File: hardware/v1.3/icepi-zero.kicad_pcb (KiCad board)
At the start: 4 copper layers, 65 x 30 mm, 160 parts, among them J1 Conn_02x20_Counter_Clockwise, J2 HDMI_C_1.3, J3 USB_C_Receptacle_USB2.0_14P, J4 USB_C_Receptacle_USB2.0_14P, J5 USB_C_Receptacle_USB2.0_14P, J6 Micro_SD_Card_Det2, SW1 SW_Push, SW2 SW_Push, U1 ECP5-CABGA256, U10 W9825G6KH, U11 W25Q128JVS, U2 TLV62569DBV, U3 TLV62569DBV, U4 TLV62569DBV, U5 PCA9306DC1, U6 FT231XQ, U7 TPD2EUSB30A, U8 TPD2EUSB30A, U9 TPD2EUSB30A, Y1 SG-8018CG 50.000000MHz

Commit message: Newest source files
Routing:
- net +3V3: track 95.9 -> 95.3 mm

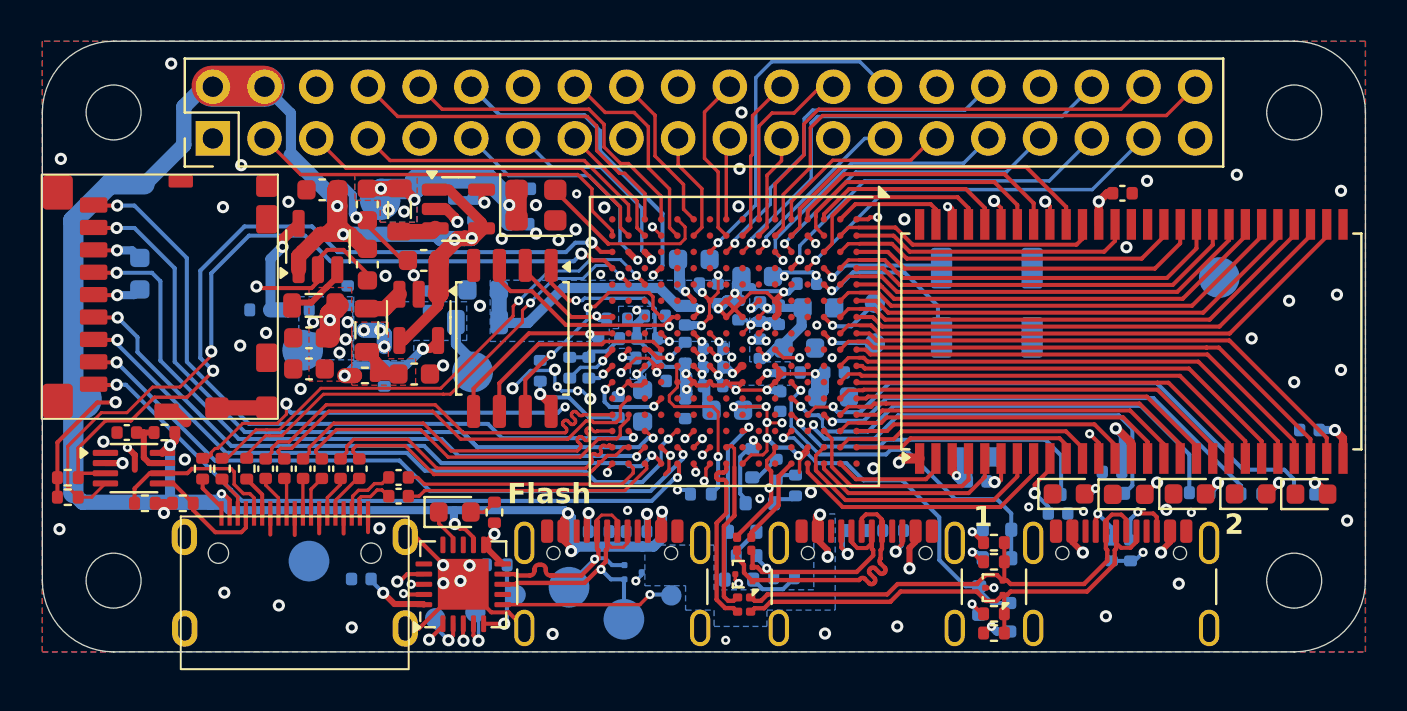
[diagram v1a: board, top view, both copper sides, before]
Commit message: Refine README
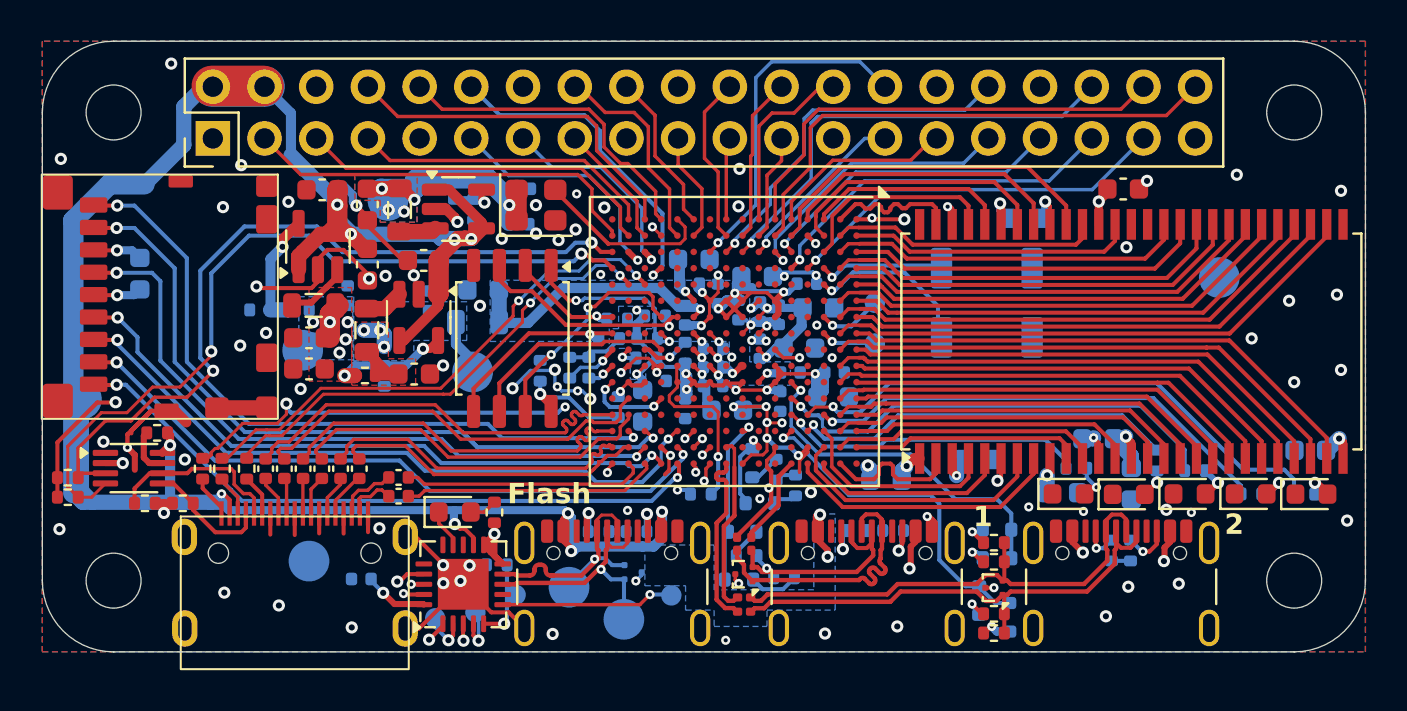
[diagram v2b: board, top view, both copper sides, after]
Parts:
- removed C37: 100pF, Capacitor_SMD:C_0402_1005Metric
- added C53: 22nF, Capacitor_SMD:C_0603_1608Metric, B.Cu at (164.2, 98.7)
- added C54: 22nF, Capacitor_SMD:C_0603_1608Metric, B.Cu at (157.4, 111.6)
- C39, C40, C41, C43, C44: value 100nF -> 22nF; footprint Capacitor_SMD:C_0402_1005Metric -> Capacitor_SMD:C_0603_1608Metric
- moved C42 7.66 mm to (169.5, 111.7), turned to -90 degrees
- moved R4 1.94 mm to (170.8, 110.6), turned to -90 degrees
- moved C40 1.77 mm to (167.9, 109.5)
- moved R1 1.31 mm to (166.8, 111.0)
- moved R2 1.10 mm to (172.6, 111.1)
- moved C43 1.08 mm to (162.0, 110.5)
- moved C41 1.04 mm to (166.1, 112.2)
- moved C39 1.00 mm to (178.3, 110.1)
- moved TP4 0.39 mm to (133.0, 97.8)
- moved R15 0.36 mm to (121.6, 109.2)
- moved C44 0.21 mm to (169.1, 97.3)
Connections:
- net FLASH_MISO renamed /Flash/FLASH_MISO
- net FLASH_MOSI renamed /Flash/FLASH_MOSI
- net JTAG_TCK renamed /USB/JTAG_TCK
- net JTAG_TDI renamed /USB/JTAG_TDI
- net JTAG_TDO renamed /USB/JTAG_TDO
- net JTAG_TMS renamed /USB/JTAG_TMS
- net ~{FLASH_CS} renamed /Flash/~{FLASH_CS}
- net ~{FLASH_RESET} renamed /Flash/~{FLASH_RESET}
- net ~{FLASH_WP} renamed /Flash/~{FLASH_WP}
- J1 pad 10: /GPIO4 -> /GPIO15
- J1 pad 11: /GPIO5 -> /GPIO17
- J1 pad 12: /GPIO6 -> /GPIO18
- J1 pad 13: /GPIO7 -> /GPIO27
- J1 pad 15: /GPIO8 -> /GPIO22
- J1 pad 16: /GPIO9 -> /GPIO23
- J1 pad 18: /GPIO10 -> /GPIO24
- J1 pad 19: /GPIO11 -> /GPIO10
- J1 pad 21: /GPIO12 -> /GPIO9
- J1 pad 22: /GPIO13 -> /GPIO25
- J1 pad 23: /GPIO14 -> /GPIO11
- J1 pad 24: /GPIO15 -> /GPIO8
- J1 pad 26: /GPIO16 -> /GPIO7
- J1 pad 27: /GPIO17 -> /GPIO0
- J1 pad 28: /GPIO18 -> /GPIO1
- J1 pad 29: /GPIO19 -> /GPIO5
- J1 pad 3: /GPIO0 -> /GPIO2
- J1 pad 31: /GPIO20 -> /GPIO6
- J1 pad 32: /GPIO21 -> /GPIO12
- J1 pad 33: /GPIO22 -> /GPIO13
- J1 pad 35: /GPIO23 -> /GPIO19
- J1 pad 36: /GPIO24 -> /GPIO16
- J1 pad 37: /GPIO25 -> /GPIO26
- J1 pad 38: /GPIO26 -> /GPIO20
- J1 pad 40: /GPIO27 -> /GPIO21
- J1 pad 5: /GPIO1 -> /GPIO3
- J1 pad 7: /GPIO2 -> /GPIO4
- J1 pad 8: /GPIO3 -> /GPIO14
- U1 pad D4: /GPIO25 -> /GPIO26
- U1 pad E1: /GPIO19 -> /GPIO5
- U1 pad E3: /GPIO22 -> /GPIO13
- U1 pad E4: /GPIO23 -> /GPIO19
- U1 pad F1: /GPIO26 -> /GPIO20
- U1 pad F2: /GPIO27 -> /GPIO21
- U1 pad F3: /GPIO20 -> /GPIO6
- U1 pad G1: /GPIO16 -> /GPIO7
- U1 pad G2: /GPIO14 -> /GPIO11
- U1 pad G3: /GPIO17 -> /GPIO0
- U1 pad H2: /GPIO15 -> /GPIO8
- U1 pad H3: /GPIO24 -> /GPIO16
- U1 pad J1: /GPIO12 -> /GPIO9
- U1 pad J2: /GPIO13 -> /GPIO25
- U1 pad J3: /GPIO21 -> /GPIO12
- U1 pad K3: /GPIO18 -> /GPIO1
- U1 pad L1: /GPIO10 -> /GPIO24
- U1 pad L2: /GPIO11 -> /GPIO10
- U1 pad M2: /GPIO9 -> /GPIO23
- U1 pad N1: /GPIO4 -> /GPIO15
- U1 pad N4: /GPIO6 -> /GPIO18
- U1 pad P1: /GPIO3 -> /GPIO14
- U1 pad P2: /GPIO8 -> /GPIO22
- U1 pad P3: /GPIO7 -> /GPIO27
- U1 pad R1: /GPIO2 -> /GPIO4
- U1 pad R2: /GPIO1 -> /GPIO3
- U1 pad R3: /GPIO5 -> /GPIO17
- U1 pad T2: /GPIO0 -> /GPIO2
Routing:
- net /GPIO27: track 25.8 -> 10.6 mm, vias 0 -> 1
- net /GPIO24: track 22.3 -> 7.88 mm, vias 1 -> 0
- net /GPIO12: track 3.80 -> 17.8 mm, vias 0 -> 1
- net /GPIO16: track 8.40 -> 22.3 mm, vias 0 -> 1
- net /GPIO14: track 5.24 -> 17.6 mm
- net /GPIO0: track 19.8 -> 8.72 mm, vias 0 -> 1
- net /GPIO25: track 19.1 -> 8.27 mm, vias 1 -> 0
- net /GPIO22: track 15.2 -> 6.18 mm, vias 1 -> 0
- net /GPIO19: track 9.09 -> 17.8 mm, vias 0 -> 1
- net /GPIO20: track 14.3 -> 22.7 mm, vias 1 -> 0
- net GND: track 90.4 -> 98.4 mm, vias 108 -> 109
- net /GPIO21: track 17.8 -> 25.8 mm, vias 1 -> 0
- net /GPIO15: track 8.11 -> 15.9 mm
- net /GPIO23: track 17.8 -> 10.1 mm, vias 1 -> 0
- net /GPIO13: track 8.27 -> 15.2 mm, vias 0 -> 1
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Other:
- board text added: "HDMI - 100ohm USB - 90ohm"
- board text added: "Icepi Zero v1.3"
- board text removed: "Icepi Zero v1.2"

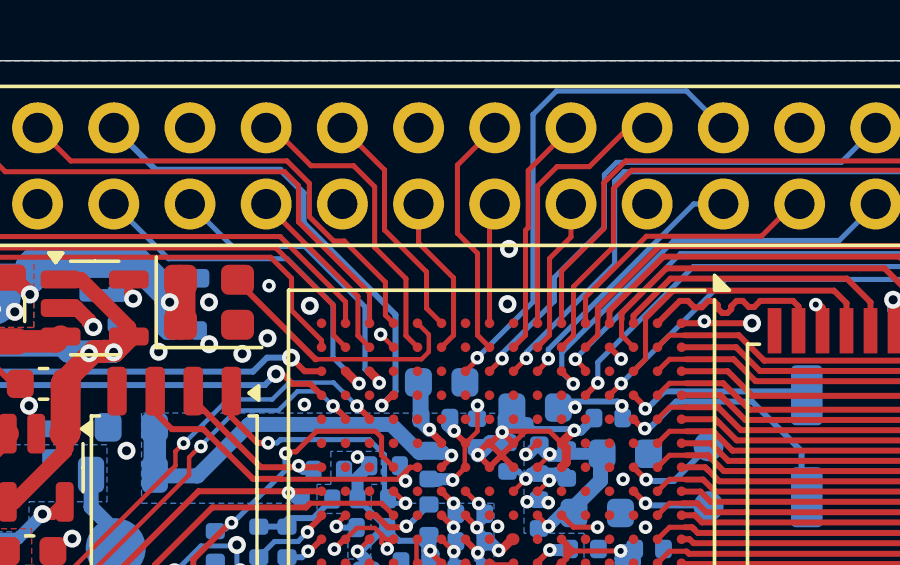
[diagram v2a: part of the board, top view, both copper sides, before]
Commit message: Change to more optimal inductor
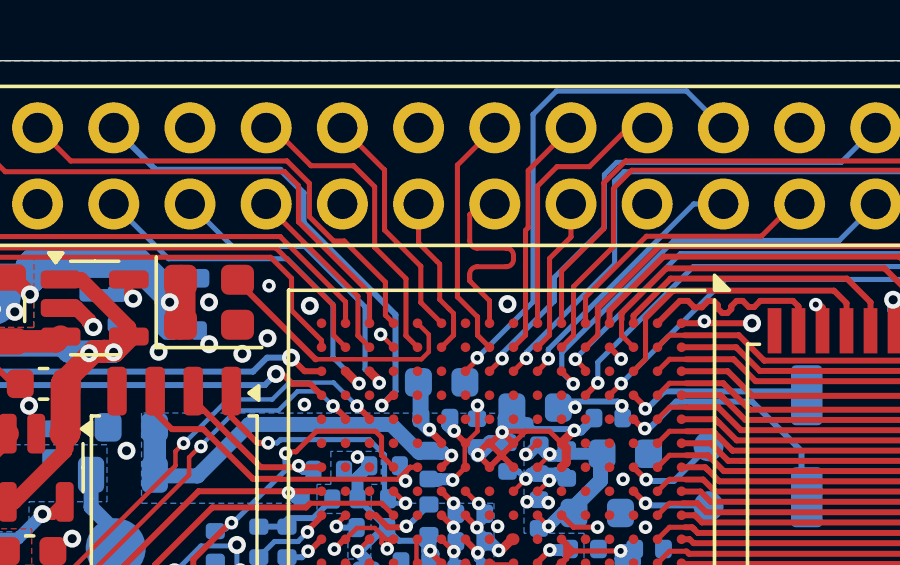
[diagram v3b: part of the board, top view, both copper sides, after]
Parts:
- L1, L2, L3: value 2.2uH -> 2.2uH 100mA+ 400mO-
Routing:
- net /GPIO9: track 3.80 -> 7.33 mm
- net GND: vias 109 -> 108
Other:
- board text added: "HDMI - 100ohm differential (coplanar waveguide 0.15mm) USB - 90ohm differential (coplanar waveguide 0.15mm)"
- board text removed: "HDMI - 100ohm USB - 90ohm"
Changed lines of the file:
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@@
 			)
 		)
-		(property "Value" "2.2uH"
+		(property "Value" "2.2uH 100mA+ 400mO-"
 			(at 0 1.55 0)
 			(layer "F.Fab")
@@
 			)
 		)
-		(property "LCSC Part #" "C1043"
+		(property "LCSC Part #" "C107322"
 			(at 0 0 0)
 			(unlocked yes)
@@
 			)
 		)
-		(property "LCSC Link" "https://lcsc.com/product-detail/Inductors-SMD_FH-CMI201209U2R2KT_C1043.html"
+		(property "LCSC Link" "https://lcsc.com/product-detail/C107322.html"
 			(at 0 0 0)
 			(unlocked yes)
@@
 			)
 		)
-		(property "Manufactuer Part Number" "CMI201209U2R2KT"
+		(property "Manufactuer Part Number" "TDK MLP2012S2R2MT0S1"
 			(at 0 0 0)
 			(unlocked yes)
@@
 			)
 		)
-		(property "Value" "2.2uH"
+		(property "Value" "2.2uH 100mA+ 400mO-"
 			(at 0 1.55 90)
 			(layer "F.Fab")
@@
 			)
 		)
-		(property "LCSC Part #" "C1043"
+		(property "LCSC Part #" "C107322"
 			(at 0 0 90)
 			(unlocked yes)
@@
 			)
 		)
-		(property "LCSC Link" "https://lcsc.com/product-detail/Inductors-SMD_FH-CMI201209U2R2KT_C1043.html"
+		(property "LCSC Link" "https://lcsc.com/product-detail/C107322.html"
 			(at 0 0 90)
 			(unlocked yes)
@@
 			)
 		)
-		(property "Manufactuer Part Number" "CMI201209U2R2KT"
+		(property "Manufactuer Part Number" "TDK MLP2012S2R2MT0S1"
 			(at 0 0 90)
 			(unlocked yes)
@@
 			)
 		)
-		(property "Value" "2.2uH"
+		(property "Value" "2.2uH 100mA+ 400mO-"
 			(at 0 1.55 90)
 			(layer "F.Fab")
@@
 			)
 		)
-		(property "LCSC Part #" "C1043"
+		(property "LCSC Part #" "C107322"
 			(at 0 0 270)
 			(unlocked yes)
@@
 			)
 		)
-		(property "LCSC Link" "https://lcsc.com/product-detail/Inductors-SMD_FH-CMI201209U2R2KT_C1043.html"
+		(property "LCSC Link" "https://lcsc.com/product-detail/C107322.html"
 			(at 0 0 270)
 			(unlocked yes)
@@
 			)
 		)
-		(property "Manufactuer Part Number" "CMI201209U2R2KT"
+		(property "Manufactuer Part Number" "TDK MLP2012S2R2MT0S1"
 			(at 0 0 270)
 			(unlocked yes)
@@
 		)
 	)
-	(gr_text "HDMI - 100ohm\nUSB - 90ohm"
+	(gr_text "HDMI - 100ohm differential (coplanar waveguide 0.15mm)\nUSB - 90ohm differential (coplanar waveguide 0.15mm)"
 		(at 150.59 88.93 0)
 		(layer "Cmts.User")
@@
 	)
 	(via
-		(at 150.25 96.27)
-		(size 0.6)
-		(drill 0.3)
-		(layers "F.Cu" "B.Cu")
-		(free yes)
-		(net 17)
-	)
-	(via
 		(at 167.15 113.1)
 		(size 0.45)
@@
 	)
 	(segment
-		(start 148.53 93.48)
-		(end 148.53 95.75)
+		(start 148.53 97.87)
+		(end 149.2 98.54)
 		(width 0.17)
 		(layer "F.Cu")
@@
 	)
 	(segment
-		(start 149.2 96.42)
-		(end 149.2 99.15)
+		(start 149.2 99.15)
+		(end 149.6 99.55)
 		(width 0.17)
 		(layer "F.Cu")
@@
 	)
 	(segment
-		(start 149.2 99.15)
-		(end 149.6 99.55)
+		(start 148.53 93.48)
+		(end 148.53 97.87)
 		(width 0.17)
 		(layer "F.Cu")
@@
 	)
 	(segment
-		(start 148.53 95.75)
-		(end 149.2 96.42)
+		(start 149.2 98.54)
+		(end 149.2 99.15)
 		(width 0.17)
 		(layer "F.Cu")
@@
 	)
 	(segment
-		(start 146.1 95.64)
-		(end 147.5 97.04)
+		(start 147.31 96.85)
+		(end 147.31 98.06)
 		(width 0.17)
 		(layer "F.Cu")
@@
 	)
 	(segment
-		(start 147.5 98.25)
-		(end 148 98.75)
+		(start 146.1 93.64)
+		(end 146.1 95.64)
 		(width 0.17)
 		(layer "F.Cu")
@@
 	)
 	(segment
-		(start 144.695 92.235)
-		(end 146.1 93.64)
+		(start 146.1 95.64)
+		(end 147.31 96.85)
 		(width 0.17)
 		(layer "F.Cu")
@@
 	)
 	(segment
-		(start 147.5 97.04)
-		(end 147.5 98.25)
+		(start 144.695 92.235)
+		(end 146.1 93.64)
 		(width 0.17)
 		(layer "F.Cu")
@@
 	)
 	(segment
-		(start 146.1 93.64)
-		(end 146.1 95.64)
+		(start 147.31 98.06)
+		(end 148 98.75)
 		(width 0.17)
 		(layer "F.Cu")
@@
 	)
 	(segment
-		(start 149.6 98.75)
-		(end 149.6 94.95)
-		(width 0.17)
+		(start 149.188 96.246689)
+		(end 150.152 96.246689)
+		(width 0.165)
+		(layer "F.Cu")
+		(net 56)
+	)
+	(segment
+		(start 150.152 96.866689)
+		(end 149.188 96.866689)
+		(width 0.165)
+		(layer "F.Cu")
+		(net 56)
+	)
+	(segment
+		(start 149.775 94.775)
+		(end 149.295 94.775)
+		(width 0.165)
+		(layer "F.Cu")
+		(net 56)
+	)
+	(segment
+		(start 148.94 97.33)
+		(end 148.94 97.34)
+		(width 0.165)
+		(layer "F.Cu")
+		(net 56)
+	)
+	(segment
+		(start 149.295 94.775)
+		(end 148.94 95.13)
+		(width 0.165)
+		(layer "F.Cu")
+		(net 56)
+	)
+	(segment
+		(start 148.94 95.13)
+		(end 148.94 95.998689)
+		(width 0.165)
+		(layer "F.Cu")
+		(net 56)
+	)
+	(segment
+		(start 148.94 97.34)
+		(end 149.6 98)
+		(width 0.165)
+		(layer "F.Cu")
+		(net 56)
+	)
+	(segment
+		(start 148.94 97.114689)
+		(end 148.94 97.238689)
+		(width 0.165)
+		(layer "F.Cu")
+		(net 56)
+	)
+	(segment
+		(start 149.6 98)
+		(end 149.6 98.75)
+		(width 0.165)
+		(layer "F.Cu")
+		(net 56)
+	)
+	(segment
+		(start 150.4 96.494689)
+		(end 150.4 96.618689)
+		(width 0.165)
+		(layer "F.Cu")
+		(net 56)
+	)
+	(segment
+		(start 148.94 97.238689)
+		(end 148.94 97.33)
+		(width 0.165)
+		(layer "F.Cu")
+		(net 56)
+	)
+	(arc
+		(start 150.4 96.618689)
+		(mid 150.327362 96.794051)
+		(end 150.152 96.866689)
+		(width 0.165)
+		(layer "F.Cu")
+		(net 56)
+	)
+	(arc
+		(start 149.188 96.866689)
+		(mid 149.012638 96.939327)
+		(end 148.94 97.114689)
+		(width 0.165)
+		(layer "F.Cu")
+		(net 56)
+	)
+	(arc
+		(start 148.94 95.998689)
+		(mid 149.012638 96.174051)
+		(end 149.188 96.246689)
+		(width 0.165)
+		(layer "F.Cu")
+		(net 56)
+	)
+	(arc
+		(start 150.152 96.246689)
+		(mid 150.327362 96.319327)
+		(end 150.4 96.494689)
+		(width 0.165)
 		(layer "F.Cu")
 		(net 56)
@@
 	)
 	(segment
-		(start 148.4 97.24)
+		(start 148.25 98.27)
+		(end 148.4 98.42)
+		(width 0.165)
+		(layer "F.Cu")
+		(net 66)
+	)
+	(segment
+		(start 148.4 98.65)
 		(end 148.4 99.15)
 		(width 0.17)
@@
 	)
 	(segment
+		(start 148.4 98.42)
+		(end 148.4 98.65)
+		(width 0.165)
+		(layer "F.Cu")
+		(net 66)
+	)
+	(segment
 		(start 147.235 96.075)
-		(end 148.4 97.24)
+		(end 147.855 96.695)
 		(width 0.17)
 		(layer "F.Cu")
@@
 	)
 	(segment
+		(start 147.94 96.78)
+		(end 147.855 96.695)
+		(width 0.165)
+		(layer "F.Cu")
+		(net 66)
+	)
+	(segment
+		(start 147.94 97.96)
+		(end 147.94 96.78)
+		(width 0.165)
+		(layer "F.Cu")
+		(net 66)
+	)
+	(segment
+		(start 148.25 98.27)
+		(end 147.94 97.96)
+		(width 0.165)
+		(layer "F.Cu")
+		(net 66)
+	)
+	(segment
 		(start 122.435 111.725)
 		(end 121.9 111.725)
@@
 		)
 	)
+	(generated
+		(type tuning_pattern)
+		(name "Tuning Pattern")
+		(layer "F.Cu")
+		(base_line
+			(pts
+				(xy 148.94 95.998689) (xy 148.94 97.33)
+			)
+		)
+		(corner_radius_percent 80)
+		(end
+			(xy 148.94 97.33)
+		)
+		(initial_side "left")
+		(last_diff_pair_gap 0.18)
+		(last_netname "/GPIO9")
+		(last_status "tuned")
+		(last_track_width 0.165)
+		(last_tuning "7.3002 mm (tuned)")
+		(max_amplitude 1.46)
+		(min_amplitude 0.01)
+		(min_spacing 0.62)
+		(origin
+			(xy 148.94 95.998689)
+		)
+		(override_custom_rules no)
+		(rounded yes)
+		(single_sided no)
+		(target_length 1000000)
+		(target_length_max 1000000)
+		(target_length_min 0)
+		(target_skew 0)
+		(target_skew_max 0.1)
+		(target_skew_min -0.1)
+		(tuning_mode "single")
+		(members "08ed9c40-dcd7-4a1e-938b-eb4a845eb960" "2e176b23-74d4-4c9b-a307-ade94eea37a9"
+			"63d8774e-ace9-400f-a2a3-d2206f7732d2" "786c9ac2-ccdb-4bec-8258-6037054dda35"
+			"9db548ab-5ea2-4913-bd18-92d6d0e9db6c" "a3bb9818-c7ad-4283-8915-5a7ff2f3a8c2"
+			"b83a10f3-cd79-4a1d-bf33-7b5e8f548227" "c6861ef7-6373-45f8-bb57-7190b48805d3"
+			"d6f7992e-88b5-49af-a6d3-e5d68d00fa77"
+		)
+	)
